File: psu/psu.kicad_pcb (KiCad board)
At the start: 2 copper layers, 100 x 100 mm, 137 parts, among them IC101 TSR 1-24150, IC102 STM32F334K8T6, IC103 TSR 1-2450, IC104 NCP161, IC105 ADuM1201, IC201 INA139, IC202 AD8605, IC203 MCP1416, IC204 AD8065, IC205 INA139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

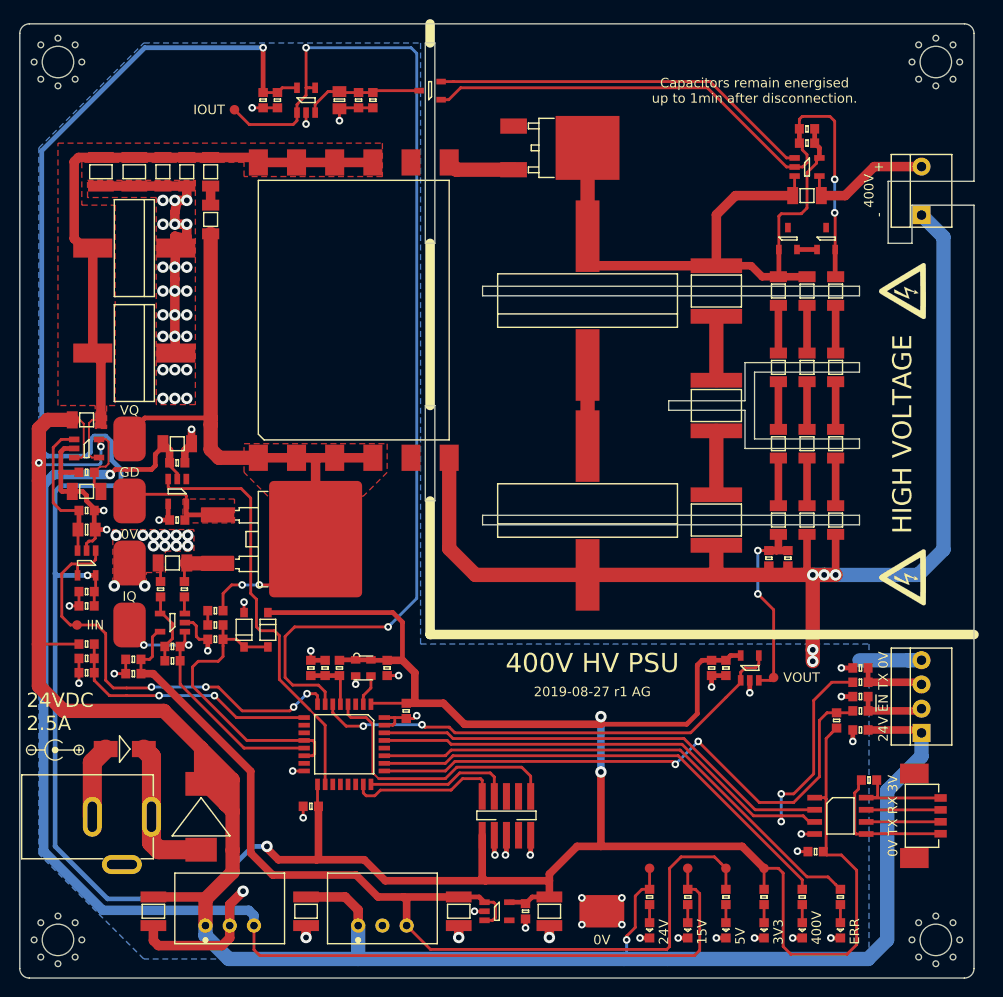
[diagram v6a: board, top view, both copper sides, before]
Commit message: Tidy up tracks. RFM r1.
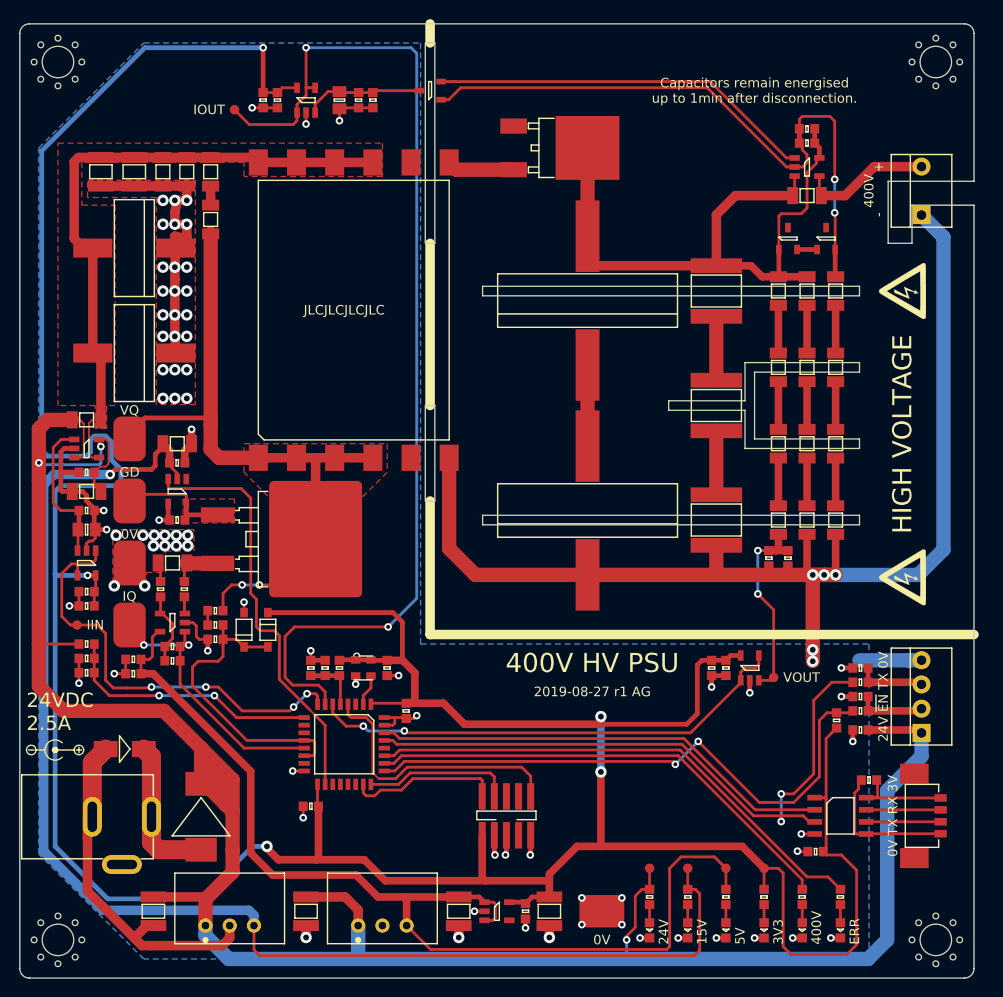
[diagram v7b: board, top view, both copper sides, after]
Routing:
- net GND: track 276.3 -> 292.8 mm, vias 85 -> 84
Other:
- board text added: "JLCJLCJLCJLC"
